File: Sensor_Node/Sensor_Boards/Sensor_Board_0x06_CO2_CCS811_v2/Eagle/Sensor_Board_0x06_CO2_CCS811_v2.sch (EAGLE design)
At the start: 28 parts, among them J1 M04_SMD_90, J4 ARDUINO_ISP, U1 CCS811, U2 ATMEGA328P_TQFP, Y1 8MHZ

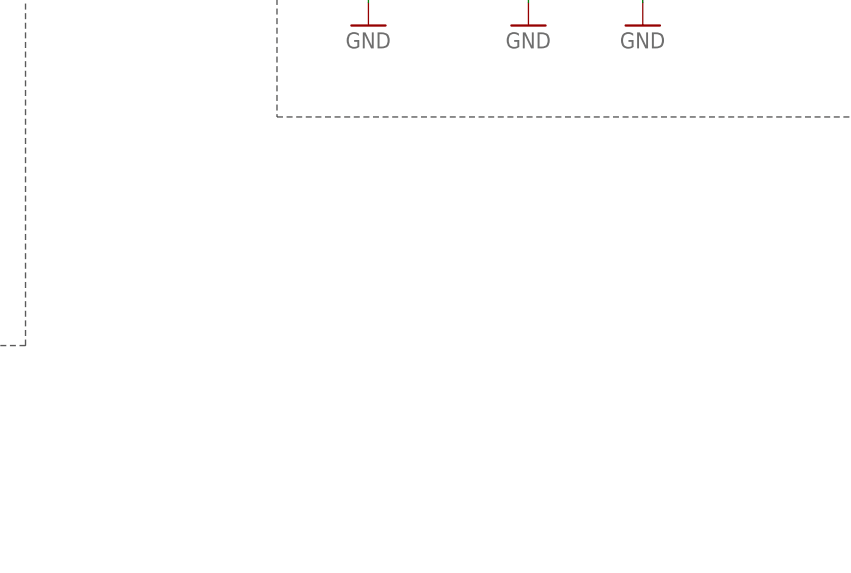
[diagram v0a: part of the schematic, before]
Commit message: Changes to C02-Board
- added power socket
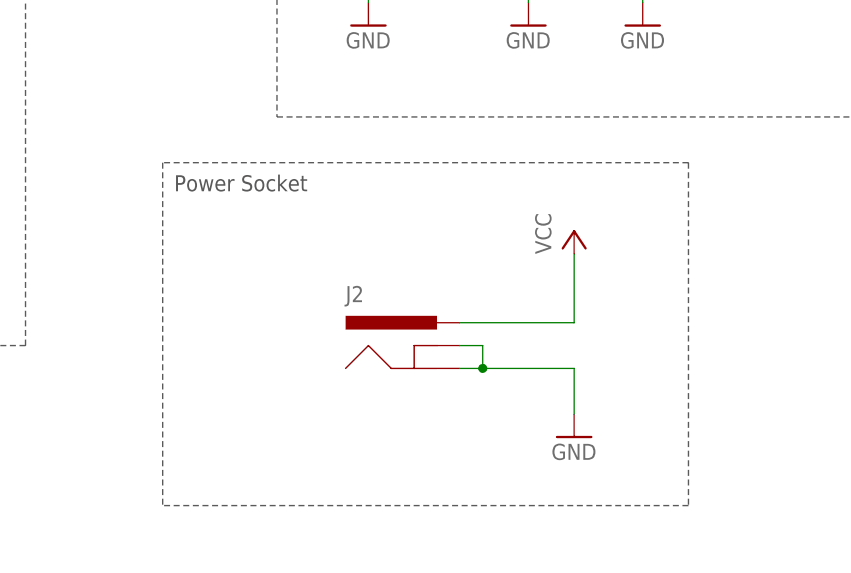
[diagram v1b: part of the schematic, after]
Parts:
- added J2: 5.5x2.1mm Barrel, wsn:POWER_JACKSMD
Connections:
- net GND: now also J2.GND, J2.GNDBREAK
- net VCC: now also J2.PWR
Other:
- note added: "Power Socket"
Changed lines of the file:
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@@
 <part name="P+16" library="supply1" deviceset="VCC" device=""/>
 <part name="GND10" library="SparkFun" deviceset="GND" device=""/>
+<part name="J2" library="wsn" deviceset="POWER_JACK" device="SMD" value="5.5x2.1mm Barrel"/>
+<part name="GND11" library="SparkFun" deviceset="GND" device=""/>
+<part name="P+17" library="supply1" deviceset="VCC" device=""/>
 </parts>
 <sheets>
@@
 <text x="140.97" y="113.665" size="1.778" layer="97">Temperaturesensor SHT31</text>
 <text x="242.57" y="113.665" size="1.778" layer="97">Pullups for I2C</text>
+<wire x1="182.88" y1="43.18" x2="124.46" y2="43.18" width="0.1524" layer="97" style="shortdash"/>
+<wire x1="182.88" y1="5.08" x2="124.46" y2="5.08" width="0.1524" layer="97" style="shortdash"/>
+<wire x1="182.88" y1="43.18" x2="182.88" y2="5.08" width="0.1524" layer="97" style="shortdash"/>
+<wire x1="124.46" y1="43.18" x2="124.46" y2="5.08" width="0.1524" layer="97" style="shortdash"/>
+<text x="125.73" y="40.005" size="1.778" layer="97">Power Socket</text>
 </plain>
 <instances>
@@
 <instance part="P+16" gate="VCC" x="147.32" y="109.22"/>
 <instance part="GND10" gate="1" x="147.32" y="58.42"/>
+<instance part="J2" gate="G$1" x="144.78" y="20.32"/>
+<instance part="GND11" gate="1" x="170.18" y="12.7"/>
+<instance part="P+17" gate="VCC" x="170.18" y="35.56"/>
 </instances>
 <busses>
@@
 <pinref part="C5" gate="G$1" pin="2"/>
 <wire x1="147.32" y1="60.96" x2="147.32" y2="86.36" width="0.1524" layer="91"/>
+</segment>
+<segment>
+<pinref part="J2" gate="G$1" pin="GND"/>
+<wire x1="157.48" y1="20.32" x2="160.02" y2="20.32" width="0.1524" layer="91"/>
+<pinref part="J2" gate="G$1" pin="GNDBREAK"/>
+<wire x1="157.48" y1="22.86" x2="160.02" y2="22.86" width="0.1524" layer="91"/>
+<wire x1="160.02" y1="22.86" x2="160.02" y2="20.32" width="0.1524" layer="91"/>
+<junction x="160.02" y="20.32"/>
+<pinref part="GND11" gate="1" pin="GND"/>
+<wire x1="160.02" y1="20.32" x2="170.18" y2="20.32" width="0.1524" layer="91"/>
+<wire x1="170.18" y1="20.32" x2="170.18" y2="15.24" width="0.1524" layer="91"/>
 </segment>
 </net>
@@
 <wire x1="147.32" y1="93.98" x2="147.32" y2="106.68" width="0.1524" layer="91"/>
 </segment>
+<segment>
+<pinref part="J2" gate="G$1" pin="PWR"/>
+<pinref part="P+17" gate="VCC" pin="VCC"/>
+<wire x1="157.48" y1="25.4" x2="170.18" y2="25.4" width="0.1524" layer="91"/>
+<wire x1="170.18" y1="25.4" x2="170.18" y2="33.02" width="0.1524" layer="91"/>
+</segment>
 </net>

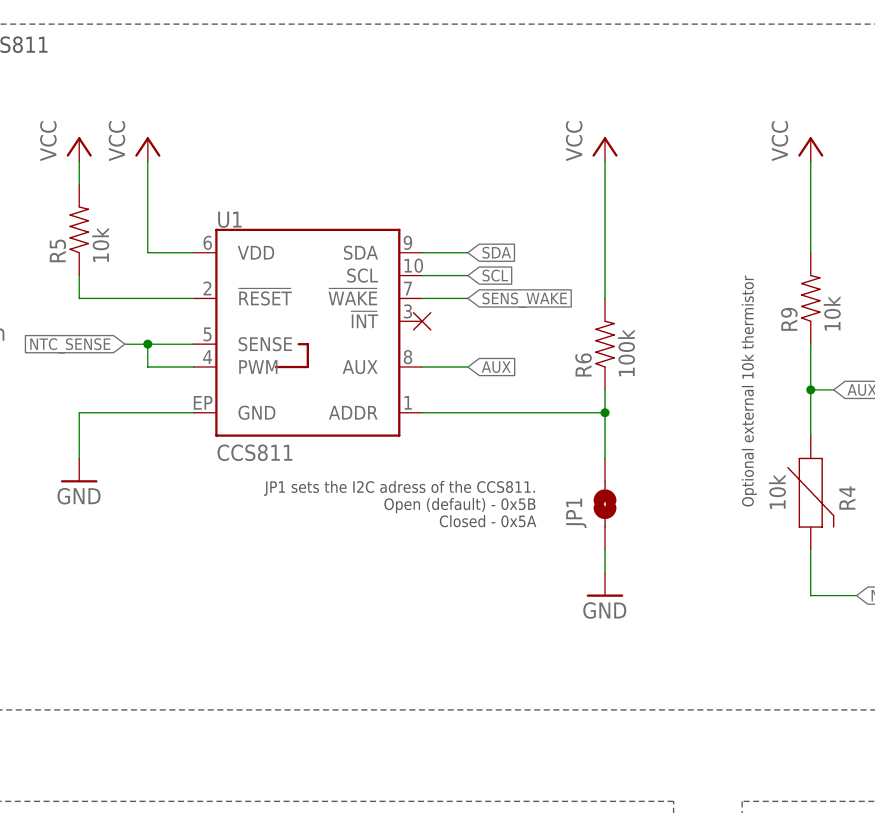
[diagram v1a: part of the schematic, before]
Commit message: Corrected mistake on C02-Board
-Connected enable-pin of sensor to GND
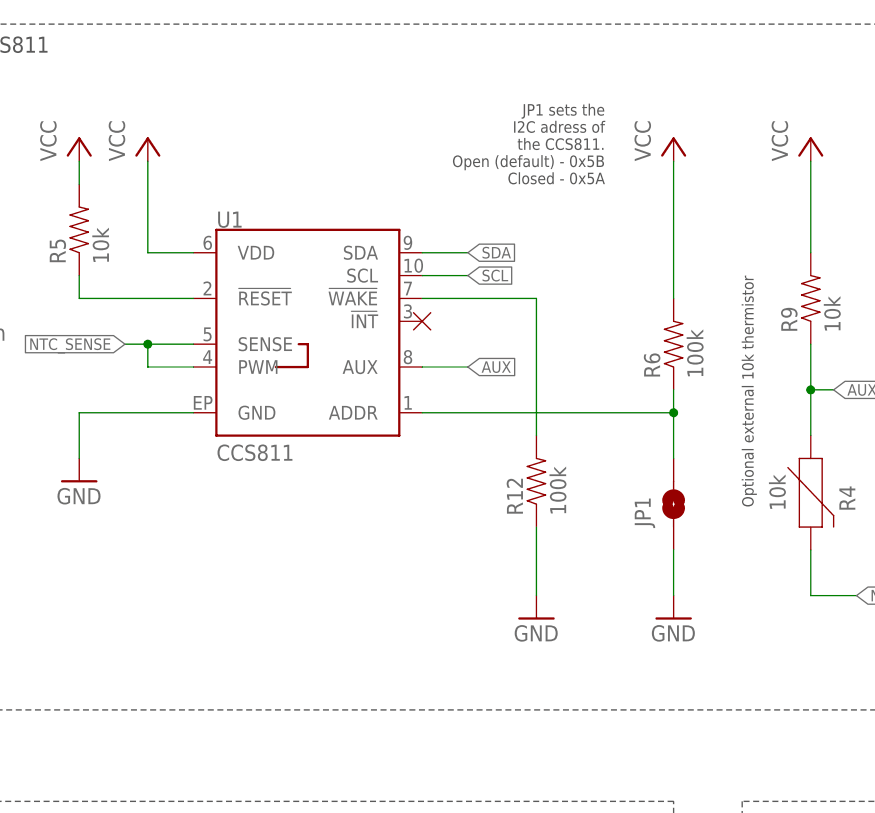
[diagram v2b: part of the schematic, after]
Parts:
- added R12: 100k, SparkFun-Passives:RESISTOR0805-RES
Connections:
- removed net SENS_WAKE: U1.!WAKE!
- new net N$5: R12.2, U1.!WAKE!
- net GND: now also R12.1
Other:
- moved on the sheet: JP1, R6
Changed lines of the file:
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@@
 <?xml version="1.0" encoding="utf-8"?>
 <!DOCTYPE eagle SYSTEM "eagle.dtd">
-<eagle version="8.5.0">
+<eagle version="8.5.2">
 <drawing>
 <settings>
@@
 <part name="GND11" library="SparkFun" deviceset="GND" device=""/>
 <part name="P+17" library="supply1" deviceset="VCC" device=""/>
+<part name="R12" library="SparkFun-Passives" deviceset="RESISTOR" device="0805-RES" value="100k"/>
+<part name="GND12" library="SparkFun" deviceset="GND" device=""/>
 </parts>
 <sheets>
@@
 <wire x1="109.22" y1="22.86" x2="109.22" y2="63.5" width="0.1524" layer="97" style="shortdash"/>
 <text x="60.198" y="60.452" size="1.778" layer="97">FTDI Pogopin Connector</text>
-<text x="215.9" y="147.32" size="1.27" layer="97" align="bottom-right">JP1 sets the I2C adress of the CCS811.
+<text x="223.52" y="185.42" size="1.27" layer="97" align="bottom-right">JP1 sets the
+I2C adress of
+the CCS811.
 Open (default) - 0x5B
 Closed - 0x5A </text>
@@
 <instance part="U$10" gate="G$1" x="99.06" y="182.88"/>
 <instance part="U1" gate="U1" x="190.5" y="170.18"/>
-<instance part="JP1" gate="G$1" x="223.52" y="149.86" smashed="yes" rot="R90">
-<attribute name="NAME" x="220.98" y="147.32" size="1.778" layer="95" font="vector" rot="R90"/>
+<instance part="JP1" gate="G$1" x="231.14" y="149.86" smashed="yes" rot="R90">
+<attribute name="NAME" x="228.6" y="147.32" size="1.778" layer="95" font="vector" rot="R90"/>
 </instance>
 <instance part="R4" gate="G$1" x="246.38" y="152.4" rot="R270"/>
 <instance part="R5" gate="G$1" x="165.1" y="180.34" rot="R90"/>
-<instance part="R6" gate="G$1" x="223.52" y="167.64" rot="R90"/>
+<instance part="R6" gate="G$1" x="231.14" y="167.64" rot="R90"/>
 <instance part="R7" gate="G$1" x="254" y="81.28" rot="R90"/>
 <instance part="R8" gate="G$1" x="279.4" y="81.28" rot="R90"/>
@@
 <instance part="P+8" gate="VCC" x="172.72" y="190.5"/>
 <instance part="GND3" gate="1" x="165.1" y="152.4"/>
-<instance part="GND4" gate="1" x="223.52" y="139.7"/>
-<instance part="P+9" gate="VCC" x="223.52" y="190.5"/>
+<instance part="GND4" gate="1" x="231.14" y="137.16"/>
+<instance part="P+9" gate="VCC" x="231.14" y="190.5"/>
 <instance part="P+10" gate="VCC" x="266.7" y="106.68"/>
 <instance part="P+11" gate="VCC" x="246.38" y="190.5"/>
@@
 <instance part="GND11" gate="1" x="170.18" y="12.7"/>
 <instance part="P+17" gate="VCC" x="170.18" y="35.56"/>
+<instance part="R12" gate="G$1" x="215.9" y="152.4" rot="R90"/>
+<instance part="GND12" gate="1" x="215.9" y="137.16"/>
 </instances>
 <busses>
@@
 <pinref part="GND4" gate="1" pin="GND"/>
 <pinref part="JP1" gate="G$1" pin="1"/>
-<wire x1="223.52" y1="142.24" x2="223.52" y2="144.78" width="0.1524" layer="91"/>
+<wire x1="231.14" y1="139.7" x2="231.14" y2="144.78" width="0.1524" layer="91"/>
 </segment>
 <segment>
@@
 <wire x1="160.02" y1="20.32" x2="170.18" y2="20.32" width="0.1524" layer="91"/>
 <wire x1="170.18" y1="20.32" x2="170.18" y2="15.24" width="0.1524" layer="91"/>
+</segment>
+<segment>
+<pinref part="R12" gate="G$1" pin="1"/>
+<pinref part="GND12" gate="1" pin="GND"/>
+<wire x1="215.9" y1="147.32" x2="215.9" y2="139.7" width="0.1524" layer="91"/>
 </segment>
 </net>
@@
 <pinref part="R6" gate="G$1" pin="2"/>
 <pinref part="P+9" gate="VCC" pin="VCC"/>
-<wire x1="223.52" y1="172.72" x2="223.52" y2="187.96" width="0.1524" layer="91"/>
+<wire x1="231.14" y1="172.72" x2="231.14" y2="187.96" width="0.1524" layer="91"/>
 </segment>
 <segment>
@@
 </segment>
 </net>
-<net name="SENS_WAKE" class="0">
-<segment>
-<pinref part="U1" gate="U1" pin="!WAKE!"/>
-<wire x1="203.2" y1="172.72" x2="208.28" y2="172.72" width="0.1524" layer="91"/>
-<label x="208.28" y="172.72" size="1.27" layer="95" xref="yes"/>
-</segment>
-</net>
 <net name="AUX" class="0">
 <segment>
@@
 <segment>
 <pinref part="U1" gate="U1" pin="ADDR"/>
-<wire x1="203.2" y1="160.02" x2="223.52" y2="160.02" width="0.1524" layer="91"/>
+<wire x1="203.2" y1="160.02" x2="231.14" y2="160.02" width="0.1524" layer="91"/>
 <pinref part="R6" gate="G$1" pin="1"/>
-<wire x1="223.52" y1="160.02" x2="223.52" y2="162.56" width="0.1524" layer="91"/>
+<wire x1="231.14" y1="160.02" x2="231.14" y2="162.56" width="0.1524" layer="91"/>
 <pinref part="JP1" gate="G$1" pin="2"/>
-<wire x1="223.52" y1="154.94" x2="223.52" y2="160.02" width="0.1524" layer="91"/>
-<junction x="223.52" y="160.02"/>
+<wire x1="231.14" y1="154.94" x2="231.14" y2="160.02" width="0.1524" layer="91"/>
+<junction x="231.14" y="160.02"/>
 </segment>
 </net>
@@
 </segment>
 </net>
+<net name="N$5" class="0">
+<segment>
+<pinref part="U1" gate="U1" pin="!WAKE!"/>
+<pinref part="R12" gate="G$1" pin="2"/>
+<wire x1="203.2" y1="172.72" x2="215.9" y2="172.72" width="0.1524" layer="91"/>
+<wire x1="215.9" y1="172.72" x2="215.9" y2="157.48" width="0.1524" layer="91"/>
+</segment>
+</net>
